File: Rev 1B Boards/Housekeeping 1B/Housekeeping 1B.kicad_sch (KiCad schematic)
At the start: 4 parts, among them J15 Banana 2P, J21 Banana 2P, J22 Banana 2P, J24 Banana 2P

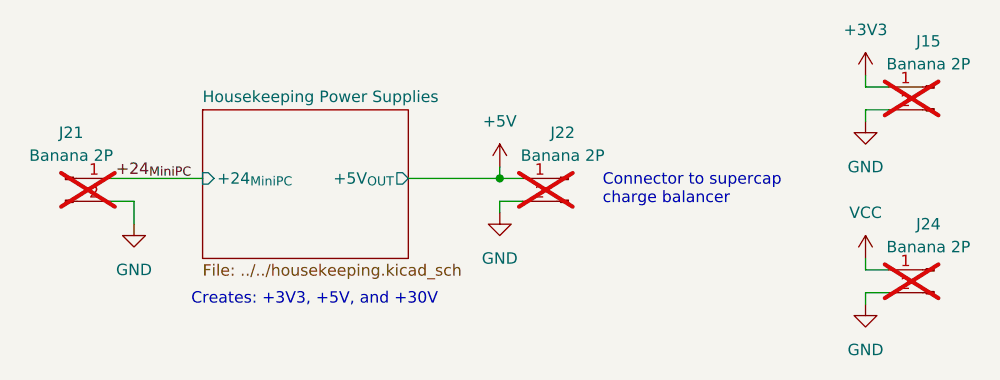
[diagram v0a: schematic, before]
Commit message: Replace most banana jacks with XT connectors
+ update library
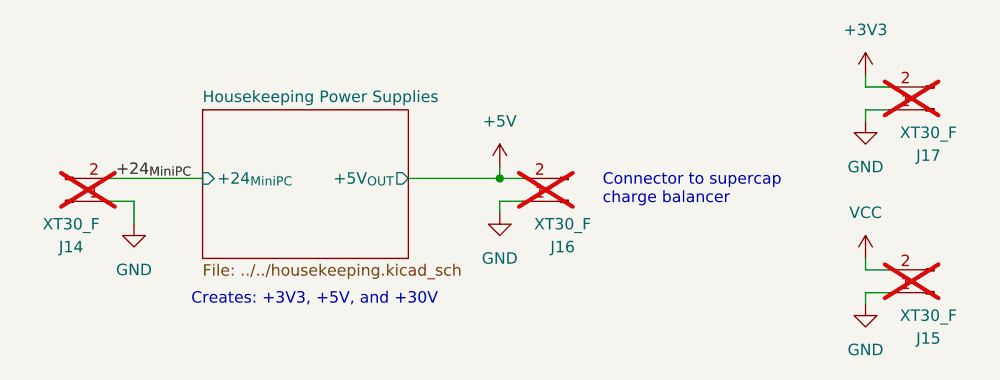
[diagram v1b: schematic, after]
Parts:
- removed J21, J22, J24: Banana 2P, Connector:Banana_Jack_2Pin, symbol Connector:Conn_01x02_Pin
- added J14, J16, J17: XT30_F, Connector_AMASS:AMASS_XT30U-F_1x02_P5.0mm_Vertical, symbol Connector:Conn_01x02_Pin
- J15: value Banana 2P -> XT30_F; footprint Connector:Banana_Jack_2Pin -> Connector_AMASS:AMASS_XT30U-F_1x02_P5.0mm_Vertical
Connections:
- net +24_{MiniPC}: now also J14.2 (Pin_2)
- net +3V3: now also J17.2 (Pin_2); no longer J15.1 (Pin_1)
- net +5V: now also J16.2 (Pin_2)
- net GND: now also J15.1 (Pin_1), J14.1 (Pin_1), J16.1 (Pin_1), J17.1 (Pin_1); no longer J15.2 (Pin_2)
- net VCC: now also J15.2 (Pin_2)
